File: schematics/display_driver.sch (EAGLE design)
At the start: 70 parts, among them IC1 TPIC6B595N, IC2 TPIC6B595N, Q1 IRF9530, Q10 BC547A, Q11 IRF9530, Q12 BC547A, Q2 IRF9530, Q3 BC547A, Q4 BC547A, Q5 IRF9530, Q6 BC547A, Q7 IRF9530, Q8 BC547A, Q9 IRF9530

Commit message: schematics: current prototyping status
Working sample :)
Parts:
- removed C_LDP, C_LSDP: (no value), wirepad:1,6/0,9
- removed Q10, Q12, Q3, Q4, Q6, Q8: BC547A, transistor-npn:BC547A
- removed R10, R2, R22, R24, R7, R8: 220, resistor:R-US_0204/7
- removed R11, R12, R4, R5: 2.2k, resistor:R-US_0204/5
- removed R20: 680R, resistor:R-US_0207/10
- removed R25, R26: 2.2k, resistor:R-US_0207/10
- added BUZZ1: F/BC40, buzzer:F/BC40
- added T1: BC547, transistor:BC547
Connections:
- removed net D7: IC1A.D7, R20.1
- removed net L_DP: C_LDP.P, C_LSDP.P, R20.2
- removed net N$10: Q7.G, R10.2, R9.1
- removed net N$11: Q8.C, R10.1
- removed net N$13: Q8.B, R4.2
- removed net N$14: Q4.B, R5.2
- removed net N$15: Q6.B, R11.2
- removed net N$16: Q3.B, R12.2
- removed net N$3: Q3.C, R2.1
- removed net N$43: Q9.G, R21.1, R22.2
- removed net N$44: Q10.C, R22.1
- removed net N$45: Q11.G, R23.1, R24.2
- removed net N$46: Q12.C, R24.1
- removed net N$48: Q12.B, R25.2
- removed net N$49: Q10.B, R26.2
- removed net N$5: Q5.G, R6.1, R7.2
- removed net N$6: Q6.C, R7.1
- removed net N$7: Q2.G, R3.1, R8.2
- removed net N$8: Q4.C, R8.1
- new net BUZZ_CTL: CONTROL.6, T1.B
- net +12V: now also BUZZ1.+
- net B_1: now also Q7.G, R9.1; no longer R4.1
- net B_2: now also Q2.G, R3.1; no longer R5.1
- net B_3: now also Q5.G, R6.1; no longer R11.1
- net B_4: now also Q1.G, R1.1; no longer R12.1
- net GND: now also T1.E; no longer Q10.E, Q12.E, Q3.E, Q4.E, Q6.E, Q8.E
- net N$2: now also BUZZ1.-, T1.C; no longer Q1.G, R1.1, R2.2
- net S_1: now also Q11.G, R23.1; no longer R25.1
- net S_2: now also Q9.G, R21.1; no longer R26.1
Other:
- moved on the sheet: A_B1, A_B2, A_B3, A_S1, C_LA, C_LB, C_LC, C_LD, C_LE, C_LF, C_LG, C_LSA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

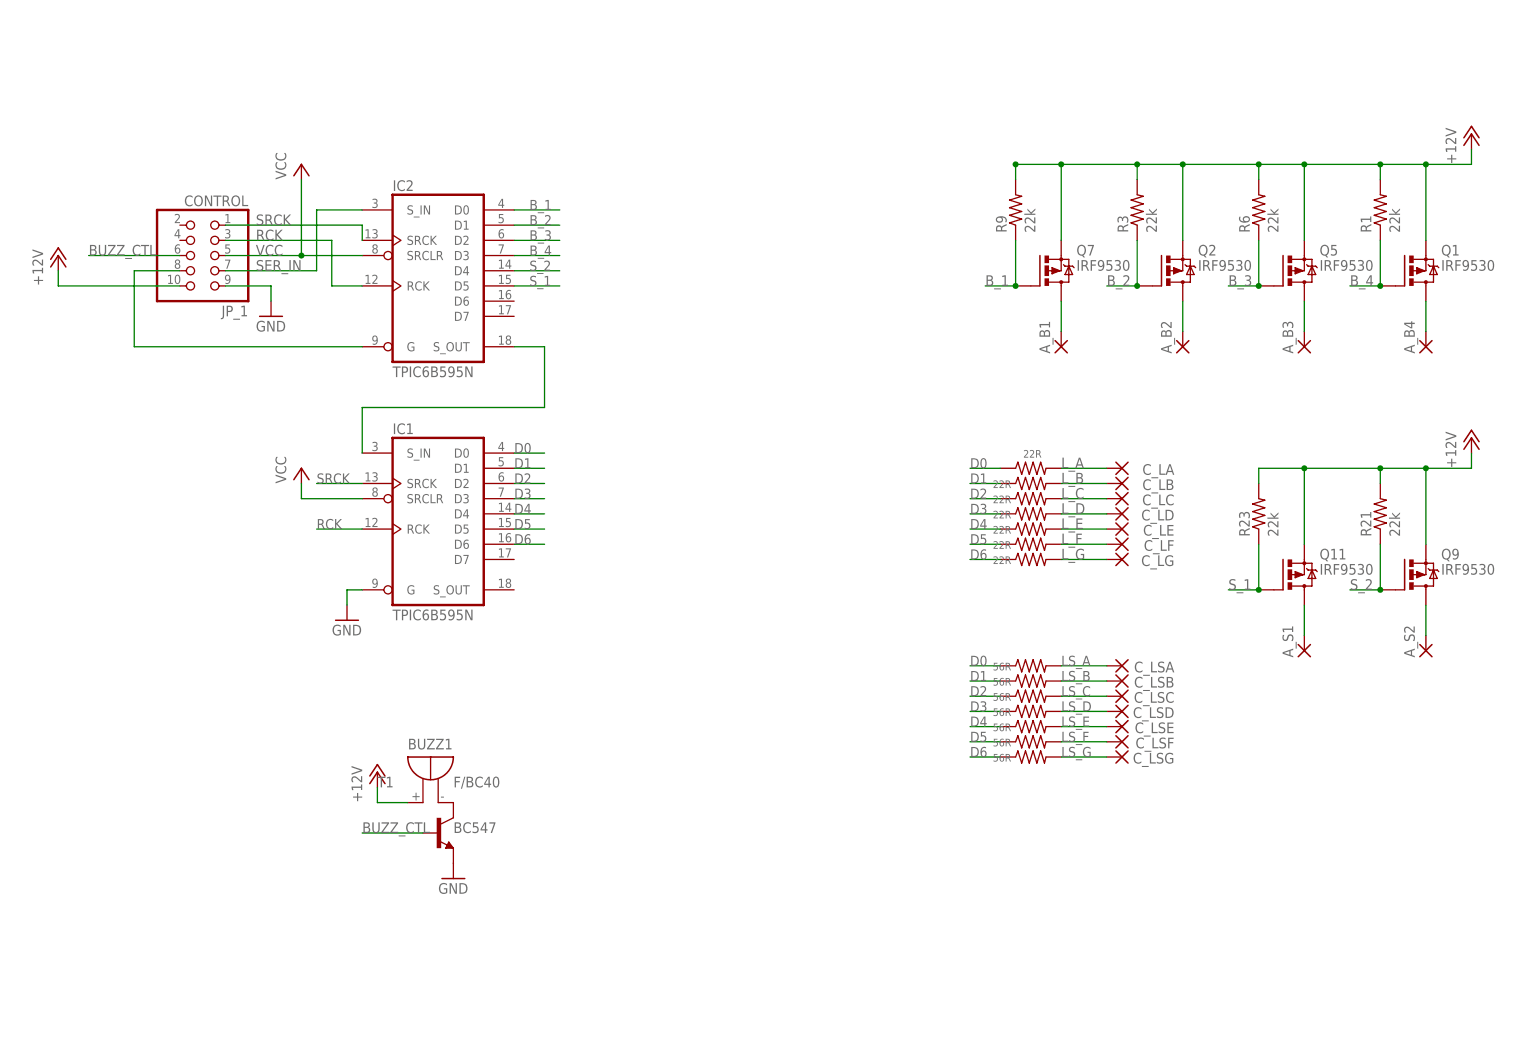
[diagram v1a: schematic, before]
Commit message: schematics: add correct MOSFET parts, improve redability
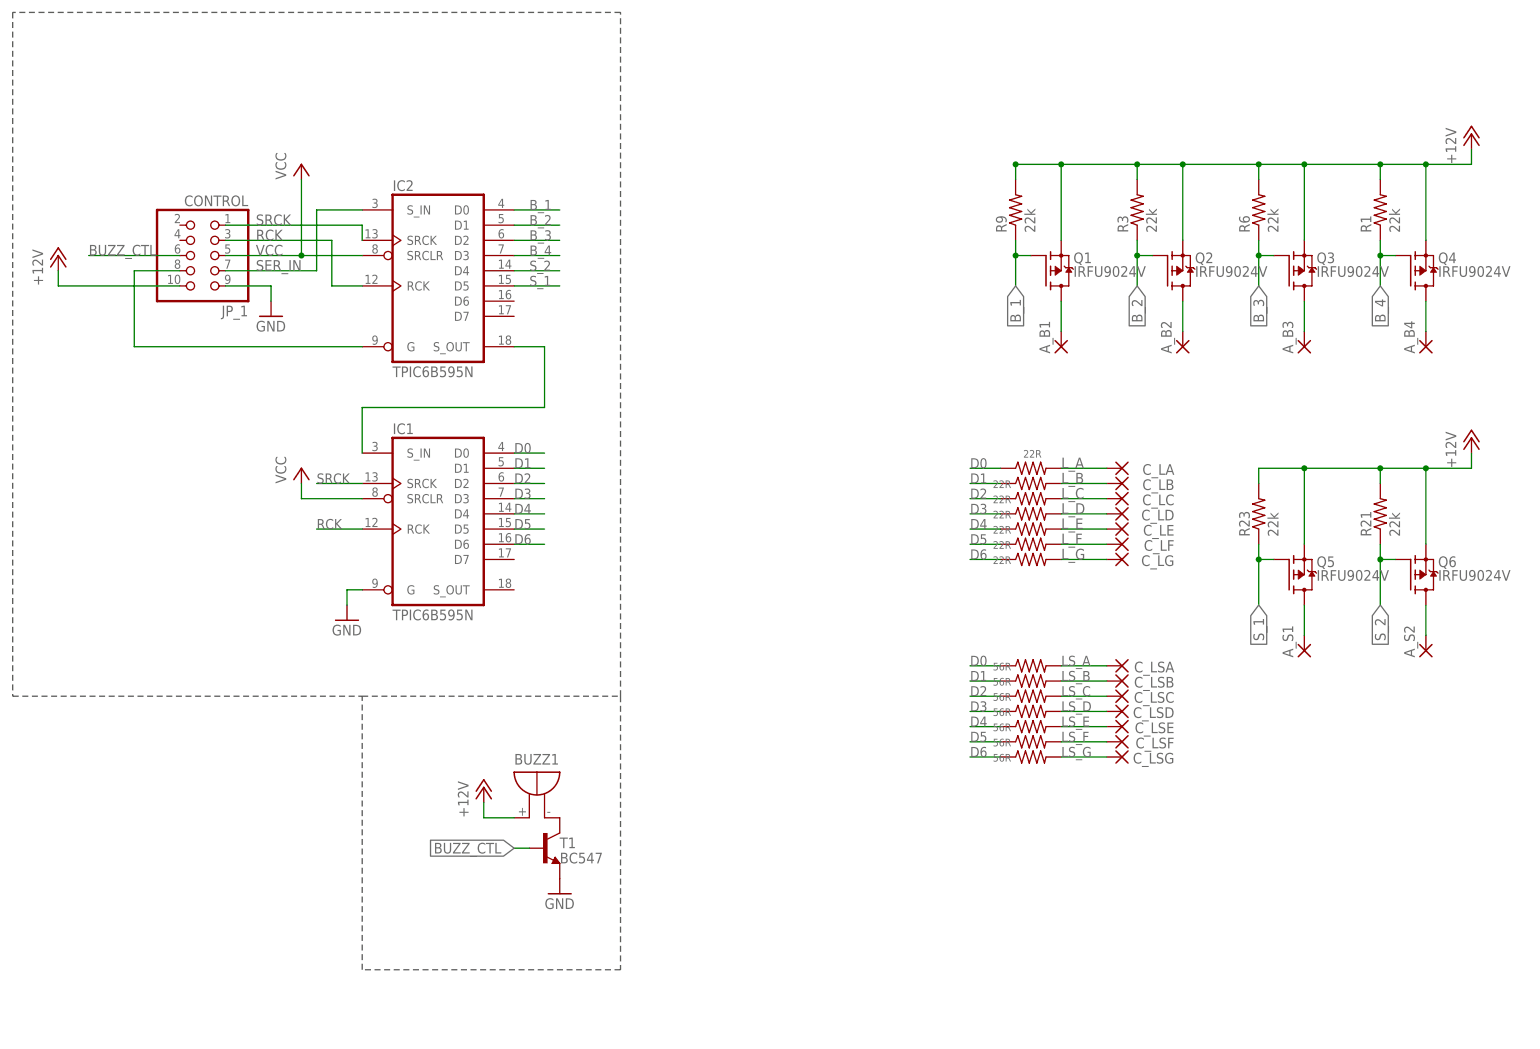
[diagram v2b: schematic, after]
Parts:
- removed Q11, Q7, Q9: IRF9530, transistor-power:IRF9530
- added Q3, Q4, Q6: IRFU9024V, MINE:IRFU9024V
- Q1, Q2, Q5: value IRF9530 -> IRFU9024V; device transistor-power:IRF9530 -> MINE:IRFU9024V
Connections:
- net +12V: now also Q3.S, Q4.S, Q6.S; no longer Q11.S, Q7.S, Q9.S
- net B_1: now also Q1.G; no longer Q7.G
- net B_3: now also Q3.G; no longer Q5.G
- net B_4: now also Q4.G; no longer Q1.G
- net N$1: now also Q1.D; no longer Q7.D
- net N$12: now also Q4.D; no longer Q1.D
- net N$42: now also Q6.D; no longer Q9.D
- net N$47: now also Q5.D; no longer Q11.D
- net N$9: now also Q3.D; no longer Q5.D
- net S_1: now also Q5.G; no longer Q11.G
- net S_2: now also Q6.G; no longer Q9.G
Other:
- moved on the sheet: BUZZ1, T1

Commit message: schematics: clean up, new design rules
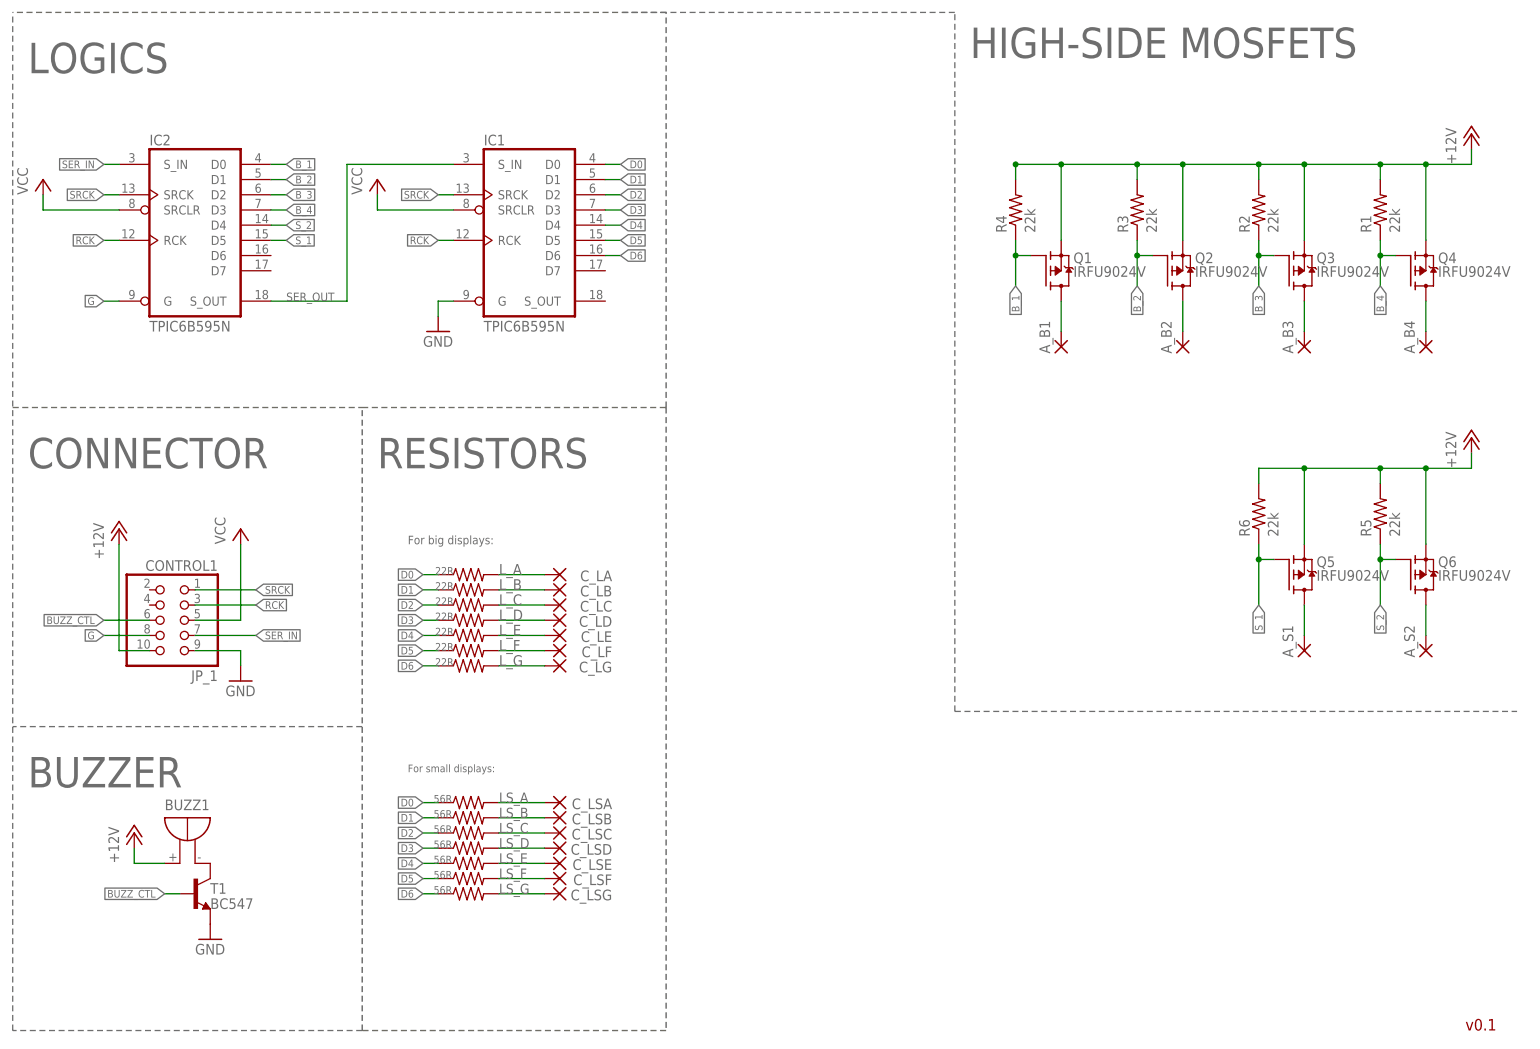
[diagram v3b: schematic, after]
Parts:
- removed CONTROL: JP_1, pinhead:PINHD-2X5
- removed R23: 22k, resistor:R-US_0204/5
- removed R27, R28, R29, R30, R31, R32, R33: 56R, resistor:R-US_0207/10
- added CONTROL1: JP_1, pinhead:PINHD-2X5
- added R10, R11, R12, R7, R8: 22R, resistor:R-US_0207/12
- added R2, R4: 22k, resistor:R-US_0204/5
- added R20: 56R, resistor:R-US_0207/10
- R14, R15, R16, R17, R18, R19: value 22R -> 56R; device resistor:R-US_0207/12 -> resistor:R-US_0207/10
- R9: value 22k -> 22R; device resistor:R-US_0204/5 -> resistor:R-US_0207/12
- renumbered R21 to R5
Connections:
- net N$17 renamed SER_OUT
- net +12V: now also CONTROL1.10, R2.2, R4.2; no longer CONTROL.10, R23.2, R9.2
- net BUZZ_CTL: now also CONTROL1.6; no longer CONTROL.6
- net B_1: now also R4.1; no longer R9.1
- net B_3: now also R2.1; no longer R6.1
- net D0: now also R14.1, R7.1; no longer R13.1, R27.1
- net D1: now also R15.1, R8.1; no longer R14.1, R28.1
- net D2: now also R16.1, R9.1; no longer R15.1, R29.1
- net D3: now also R10.1, R17.1; no longer R16.1, R30.1
- net D4: now also R11.1, R18.1; no longer R17.1, R31.1
- net D5: now also R12.1, R19.1; no longer R18.1, R32.1
- net D6: now also R13.1, R20.1; no longer R19.1, R33.1
- net G: now also CONTROL1.8; no longer CONTROL.8
- net GND: now also CONTROL1.9; no longer CONTROL.9
- net LS_A: now also R14.2; no longer R27.2
- net LS_B: now also R15.2; no longer R28.2
- net LS_C: now also R16.2; no longer R29.2
- net LS_D: now also R17.2; no longer R30.2
- net LS_E: now also R18.2; no longer R31.2
- net LS_F: now also R19.2; no longer R32.2
- net LS_G: now also R20.2; no longer R33.2
- net L_A: now also R7.2; no longer R13.2
- net L_B: now also R8.2; no longer R14.2
- net L_C: now also R9.2; no longer R15.2
- net L_D: now also R10.2; no longer R16.2
- net L_E: now also R11.2; no longer R17.2
- net L_F: now also R12.2; no longer R18.2
- net L_G: now also R13.2; no longer R19.2
- net RCK: now also CONTROL1.3; no longer CONTROL.3
- net SER_IN: now also CONTROL1.7; no longer CONTROL.7
- net SRCK: now also CONTROL1.1; no longer CONTROL.1
- net S_1: now also R6.1; no longer R23.1
- net VCC: now also CONTROL1.5; no longer CONTROL.5
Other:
- note added: "BUZZER"
- note added: "CONNECTOR"
- note added: "For big displays:"
- note added: "For small displays:"
- note added: "HIGH-SIDE MOSFETS"
- note added: "LOGICS"
- note added: "RESISTORS"
- moved on the sheet: BUZZ1, C_LA, C_LB, C_LC, C_LD, C_LE, C_LF, C_LG, C_LSA, C_LSB, C_LSC, C_LSD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
